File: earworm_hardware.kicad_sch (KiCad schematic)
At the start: 0 parts

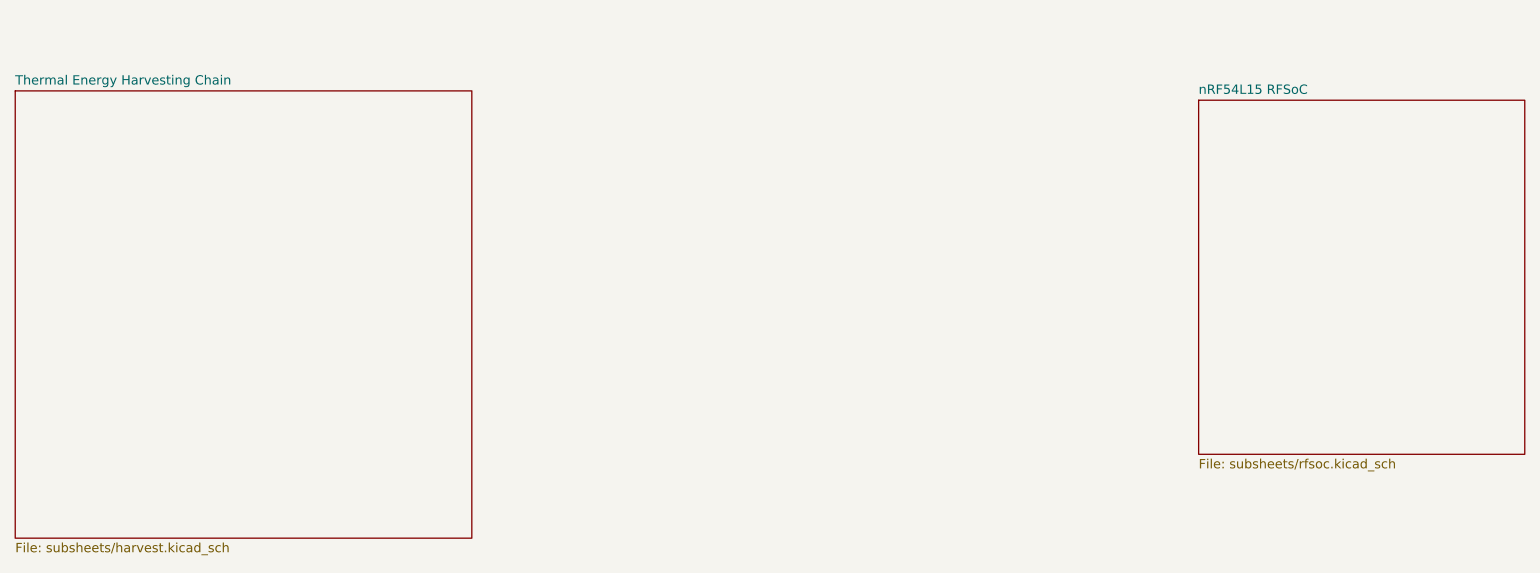
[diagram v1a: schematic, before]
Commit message: Added first draft of thermal energy harvesting chain. Need to run through ERC and fix errors
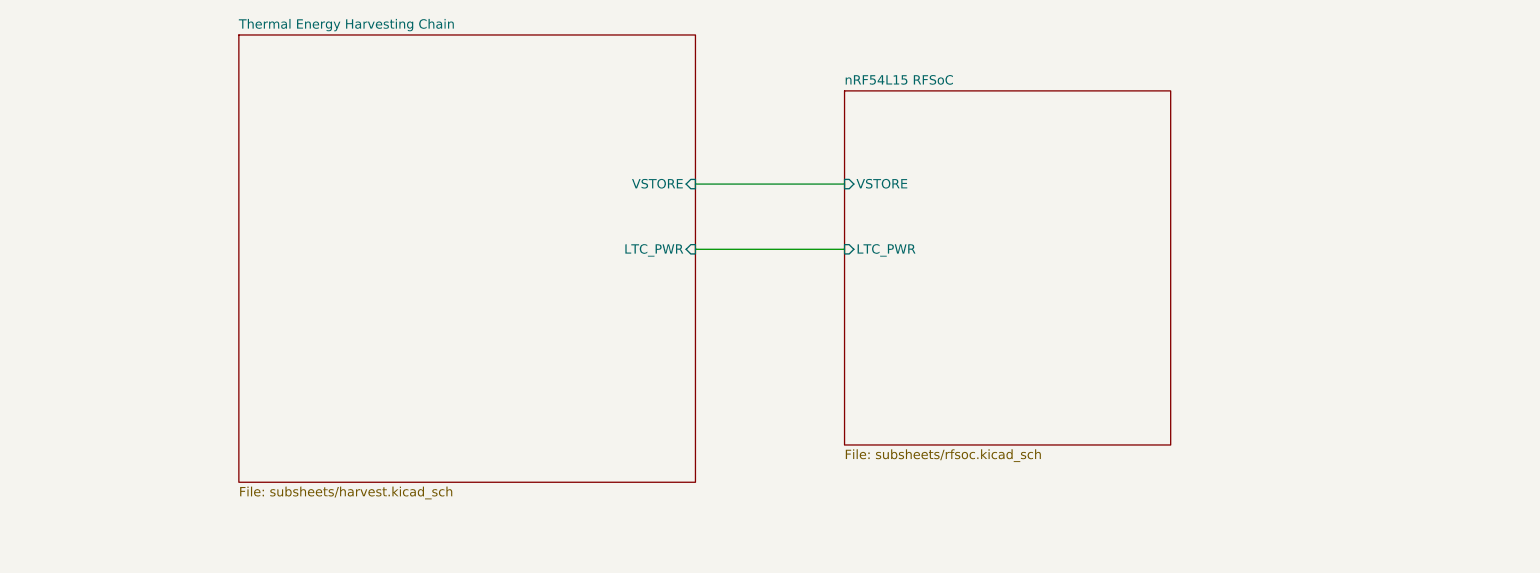
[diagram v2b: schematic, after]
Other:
- sheet Thermal Energy Harvesting Chain ports: added LTC_PWR, VSTORE; removed none
- sheet nRF54L15 RFSoC ports: added LTC_PWR, VSTORE; removed none
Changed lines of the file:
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@@
 	(generator_version "8.0")
 	(paper "A4")
+	(wire
+		(pts
+			(xy 148.59 83.82) (xy 168.91 83.82)
+		)
+		(stroke
+			(width 0)
+			(type default)
+		)
+	)
+	(wire
+		(pts
+			(xy 148.59 92.71) (xy 168.91 92.71)
+		)
+		(stroke
+			(width 0)
+			(type default)
+		)
+	)
 	(sheet
-		(at 55.88 71.12)
+		(at 86.36 63.5)
 		(size 62.23 60.96)
 		(fields_autoplaced yes)
@@
 		)
 		(property "Sheetname" "Thermal Energy Harvesting Chain"
-			(at 55.88 70.4084 0)
+			(at 86.36 62.7884 0)
 			(effects
 				(font
@@
 		)
 		(property "Sheetfile" "subsheets/harvest.kicad_sch"
-			(at 55.88 132.6646 0)
+			(at 86.36 125.0446 0)
 			(effects
 				(font
@@
 				)
 				(justify left top)
+			)
+		)
+		(pin "VSTORE" input
+			(at 148.59 83.82 0)
+			(effects
+				(font
+					(size 1.27 1.27)
+				)
+				(justify right)
+			)
+		)
+		(pin "LTC_PWR" input
+			(at 148.59 92.71 0)
+			(effects
+				(font
+					(size 1.27 1.27)
+				)
+				(justify right)
 			)
 		)
@@
 	)
 	(sheet
-		(at 217.17 72.39)
+		(at 168.91 71.12)
 		(size 44.45 48.26)
 		(fields_autoplaced yes)
@@
 		)
 		(property "Sheetname" "nRF54L15 RFSoC"
-			(at 217.17 71.6784 0)
+			(at 168.91 70.4084 0)
 			(effects
 				(font
@@
 		)
 		(property "Sheetfile" "subsheets/rfsoc.kicad_sch"
-			(at 217.17 121.2346 0)
+			(at 168.91 119.9646 0)
 			(effects
 				(font
@@
 			)
 		)
+		(pin "VSTORE" input
+			(at 168.91 83.82 180)
+			(effects
+				(font
+					(size 1.27 1.27)
+				)
+				(justify left)
+			)
+		)
+		(pin "LTC_PWR" input
+			(at 168.91 92.71 180)
+			(effects
+				(font
+					(size 1.27 1.27)
+				)
+				(justify left)
+			)
+		)
